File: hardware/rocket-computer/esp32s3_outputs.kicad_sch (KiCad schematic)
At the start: 43 parts, among them J5 Conn_01x04, SW3 R-667995, U11 GD5F2GQ5UEYIGR, U13 GD25Q128ESIG, U14 479480001, U15 ESP32-S3RH2, U29 TPS22810DRVR, Y1 ABS07-32.768KHZ-T, Y2 ECS-400-10-37B2-CKY-TR

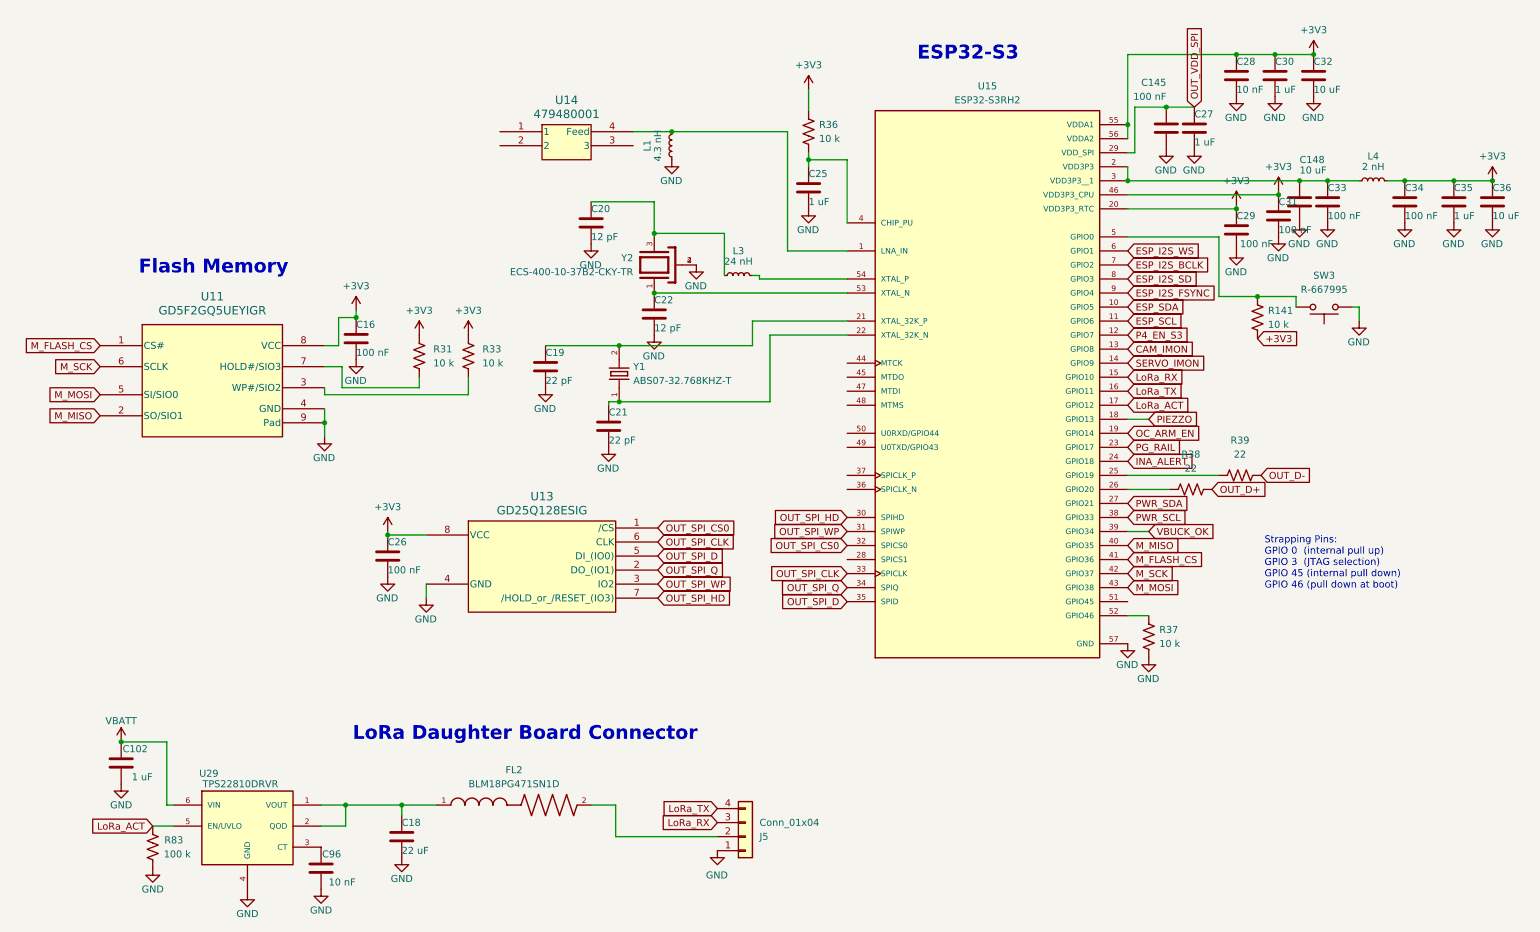
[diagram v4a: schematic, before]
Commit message: rocket-computer: the V10 ERC error floor goes from 62 to 0 without touching a net (#680)
The 62 errors were noise that buried anything real: 38 deliberately unused
pins without no-connect flags, 12 power inputs on nets with no power output,
and 12 pin-type clashes from shared symbols whose grounds were typed as power
outputs and whose tied-off open-drain pins were typed as outputs.

Pin types are fixed in the shared library and in every cached copy that
instantiates the symbol: IC grounds are power inputs; one power output per
net (eFuse OUT 17 drives VBATT, the P4's internal-LDO outputs drive VDDO_*,
the S3's VDD_SPI is a regulator output in the in-package-flash configuration
every board here uses); tied-off open-drain pins are passive; the TPS62152's
hidden thermal pad is no longer a hidden power input (the source of the
GND/PGND multiple-net-names warning). Six PWR_FLAGs mark the nets fed
through an inductor or resistor, plus GND. 38 no-connect flags. AONR21321
joins the library. Six stray wire stubs and an orphan VBATT symbol go.

Netlists are byte-identical before and after on all five boards touched.
V10 62 -> 0 errors; through the shared symbols the mini goes 40 -> 33, the
base stations 47 -> 46 and 40 -> 39, the LoRa daughterboard 34 -> 33. The
mini's remainder is its own (QMC5883P/BMP581 grounds, its flags) and is
listed in the note.

Co-Authored-By: Claude Fable 5.1 <noreply@anthropic.com>
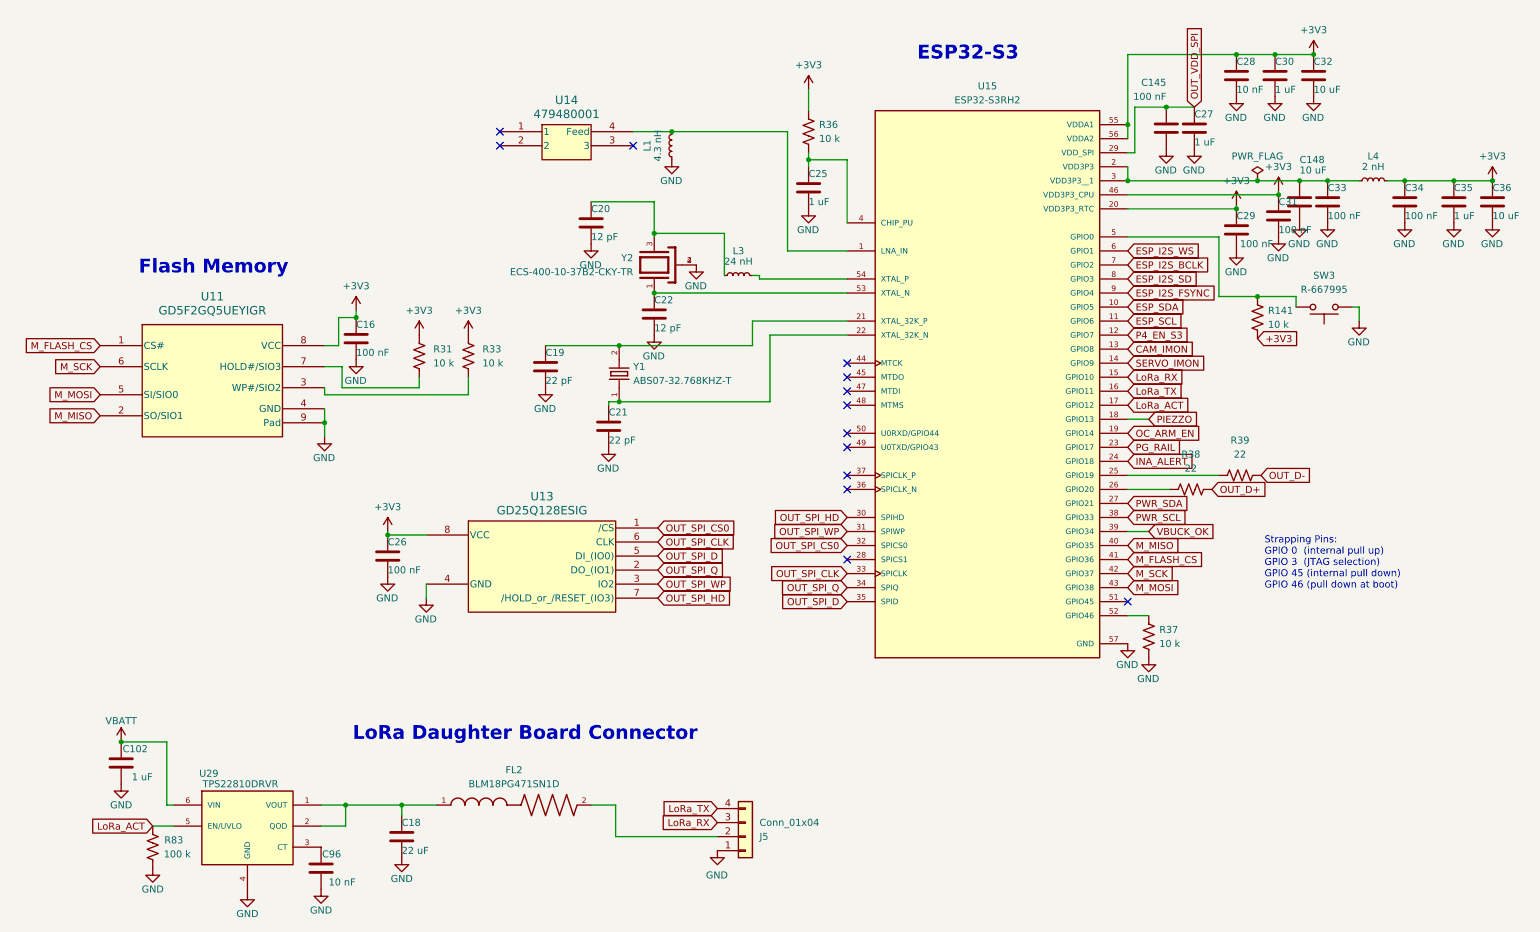
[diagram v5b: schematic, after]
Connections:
- no-connect marks 0 -> 13
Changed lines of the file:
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@@
 	(wire
 		(pts
-			(xy 212.725 40.64) (xy 243.84 40.64)
+			(xy 212.725 40.64) (xy 236.22 40.64)
+		)
+		(stroke
+			(width 0)
+			(type default)
+		)
+	)
+	(wire
+		(pts
+			(xy 236.22 40.64) (xy 243.84 40.64)
 		)
 		(stroke
@@
 		)
 	)
+	(junction
+		(at 236.22 40.64)
+		(diameter 0)
+		(color 0 0 0 0)
+	)
+	(symbol
+		(lib_id "power:PWR_FLAG")
+		(at 236.22 40.64 0)
+		(unit 1)
+		(body_style 1)
+		(exclude_from_sim no)
+		(in_bom yes)
+		(on_board yes)
+		(in_pos_files yes)
+		(dnp no)
+		(property "Reference" "#FLG02"
+			(at 236.22 38.735 0)
+			(hide yes)
+			(show_name no)
+			(do_not_autoplace no)
+			(effects
+				(font
+					(size 1.27 1.27)
+				)
+			)
+		)
+		(property "Value" "PWR_FLAG"
+			(at 236.22 36.195 0)
+			(show_name no)
+			(do_not_autoplace no)
+			(effects
+				(font
+					(size 1.27 1.27)
+				)
+			)
+		)
+		(property "Footprint" ""
+			(at 236.22 40.64 0)
+			(hide yes)
+			(show_name no)
+			(do_not_autoplace no)
+			(effects
+				(font
+					(size 1.27 1.27)
+				)
+			)
+		)
+		(property "Datasheet" ""
+			(at 236.22 40.64 0)
+			(hide yes)
+			(show_name no)
+			(do_not_autoplace no)
+			(effects
+				(font
+					(size 1.27 1.27)
+				)
+			)
+		)
+		(property "Description" "Special symbol for telling ERC where power comes from"
+			(at 236.22 40.64 0)
+			(hide yes)
+			(show_name no)
+			(do_not_autoplace no)
+			(effects
+				(font
+					(size 1.27 1.27)
+				)
+			)
+		)
+		(pin "1"
+		)
+		(instances
+			(project "rocket-computer"
+				(path "/ae61c2c4-72e9-4776-93ae-2e716b9dc70f/eab70588-b031-4461-adac-e038e88381cb"
+					(reference "#FLG02")
+					(unit 1)
+				)
+			)
+		)
+	)
+	(no_connect
+		(at 99.06 31.75)
+	)
+	(no_connect
+		(at 99.06 34.29)
+	)
+	(no_connect
+		(at 123.19 34.29)
+	)
+	(no_connect
+		(at 161.925 109.22)
+	)
+	(no_connect
+		(at 161.925 96.52)
+	)
+	(no_connect
+		(at 161.925 93.98)
+	)
+	(no_connect
+		(at 161.925 73.66)
+	)
+	(no_connect
+		(at 161.925 76.2)
+	)
+	(no_connect
+		(at 161.925 78.74)
+	)
+	(no_connect
+		(at 161.925 81.28)
+	)
+	(no_connect
+		(at 212.725 116.84)
+	)
+	(no_connect
+		(at 161.925 88.9)
+	)
+	(no_connect
+		(at 161.925 86.36)
+	)
 )
